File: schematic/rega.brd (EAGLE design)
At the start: 100 x 100 mm, 42 parts, among them IC1 ESP8266_ESP-12, K1 FRS1B, K2 351, K3 351, Q100 BSS123, Q101 2N7002, Q102 2N7002, X1 GMSTBA2, X2 GMSTBA2

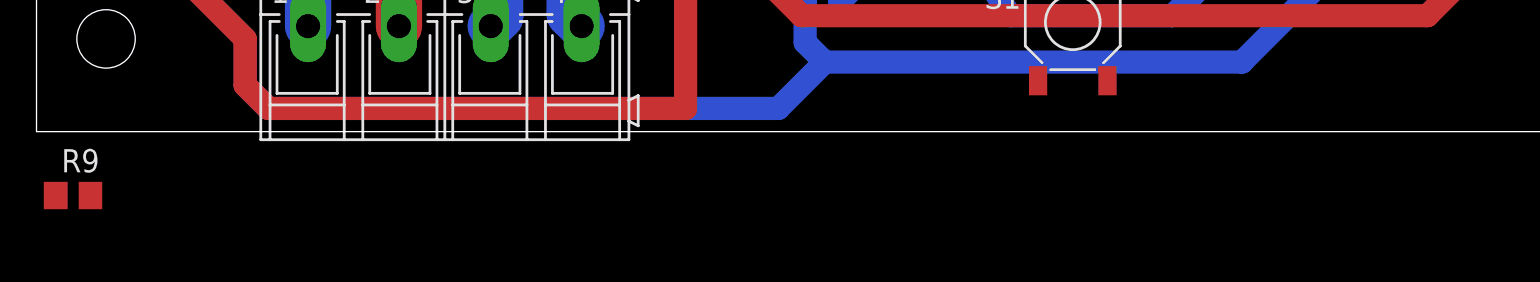
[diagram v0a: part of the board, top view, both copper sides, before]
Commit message: HW add missing resistor GPIO2 High
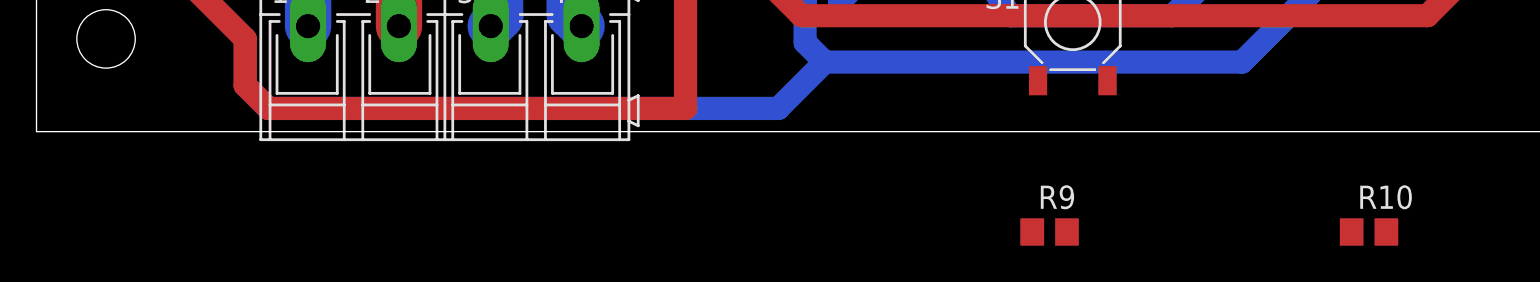
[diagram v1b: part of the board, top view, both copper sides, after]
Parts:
- added R10: 10K, rcl:R0805
- moved R9 53.5 mm to (55.5, -5.50)
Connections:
- net +3V3: now also R10.2
- net GPIO2: now also R10.1
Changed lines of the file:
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@@
 </element>
 <element name="TR1" library="trafo" package="PT13-2" value="" x="71.12" y="63.5" rot="R270"/>
-<element name="R9" library="rcl" package="R0805" value="10K" x="2" y="-3.5"/>
+<element name="R9" library="rcl" package="R0805" value="10K" x="55.5" y="-5.5"/>
+<element name="R10" library="rcl" package="R0805" value="10K" x="73" y="-5.5"/>
 </elements>
 <signals>
@@
 <wire x1="31.9" y1="15.43" x2="31.75" y2="15.28" width="1.27" layer="16"/>
 <contactref element="R9" pad="2"/>
-<wire x1="2.95" y1="-3.5" x2="11.43" y2="2.54" width="0" layer="19" extent="1-1"/>
+<contactref element="R10" pad="2"/>
+<wire x1="56.45" y1="-5.5" x2="11.43" y2="2.54" width="0" layer="19" extent="1-1"/>
+<wire x1="73.95" y1="-5.5" x2="56.45" y2="-5.5" width="0" layer="19" extent="1-1"/>
 </signal>
 <signal name="N$4">
@@
 <signal name="GPIO2">
 <contactref element="IC1" pad="3"/>
+<contactref element="R10" pad="1"/>
+<wire x1="72.05" y1="-5.5" x2="51.76" y2="17.43" width="0" layer="19" extent="1-1"/>
 </signal>
 <signal name="N$11">
@@
 <contactref element="S1" pad="4"/>
 <wire x1="58.67" y1="9.19" x2="51.76" y2="19.43" width="0" layer="19" extent="1-1"/>
-<wire x1="1.05" y1="-3.5" x2="51.76" y2="19.43" width="0" layer="19" extent="1-1"/>
+<wire x1="54.55" y1="-5.5" x2="51.76" y2="19.43" width="0" layer="19" extent="1-1"/>
 </signal>
 </signals>
